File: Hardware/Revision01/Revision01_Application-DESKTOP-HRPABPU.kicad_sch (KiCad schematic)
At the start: 82 parts, among them J10 StrainConn, J11 StrainConn, J12 StrainConn, J15 Conn_01x09, J5 StrainConn, J6 StrainConn, J7 StrainConn, J8 StrainConn, J9 StrainConn, Q1 PMOS, Q2 NMOS, Q3 PMOS, U3 MPU-6500

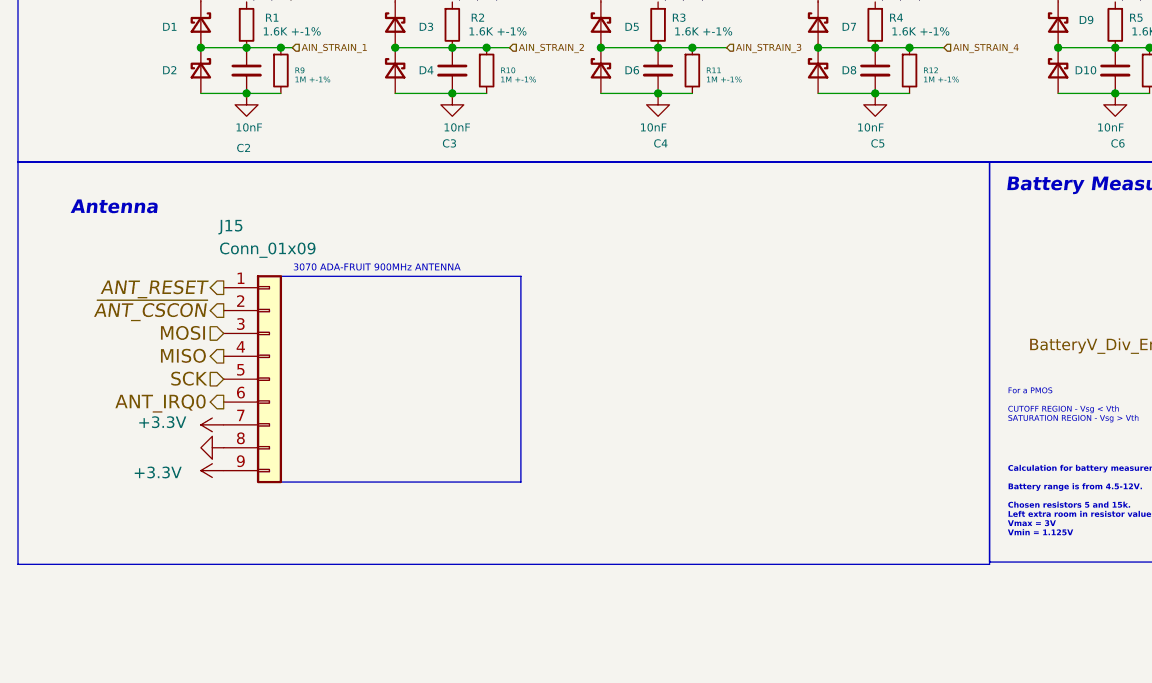
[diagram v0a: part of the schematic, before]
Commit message: review 2 implemented
- Made mounting holes symmetrical
- Buck enable 0 ohm resistor error fixed
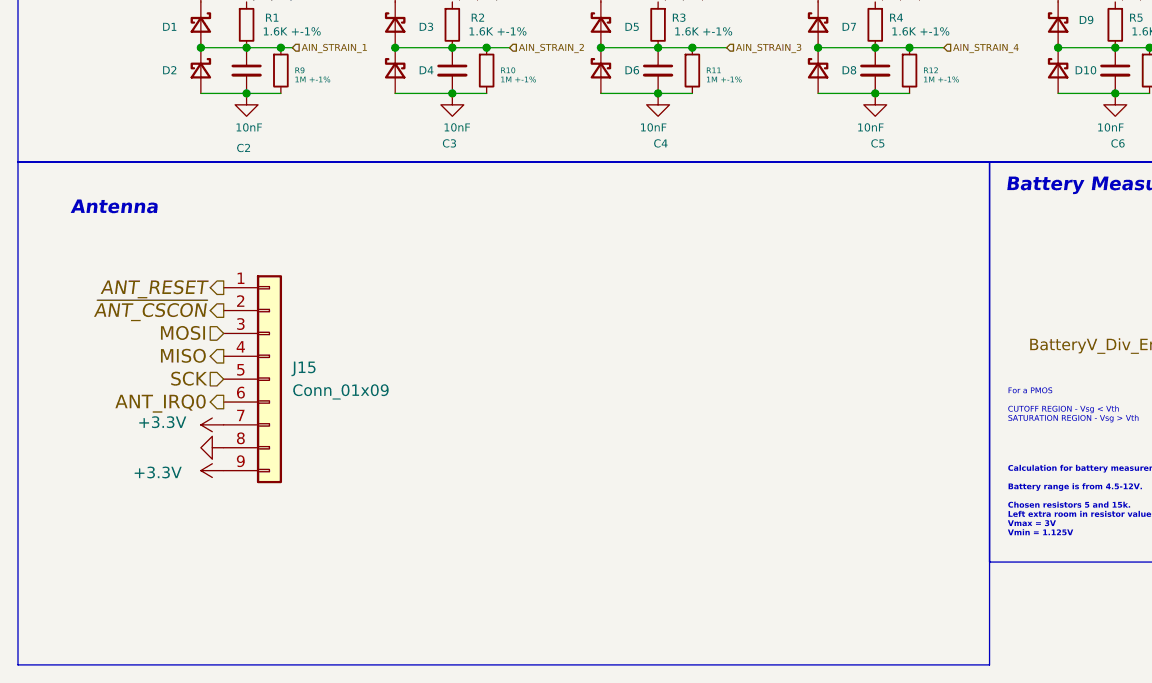
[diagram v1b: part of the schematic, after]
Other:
- note removed: "3070 ADA-FRUIT 900MHz ANTENNA"
